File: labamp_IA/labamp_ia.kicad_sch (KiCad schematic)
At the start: 35 parts, among them J1 Conn_02x06_Odd_Even, J2 Conn_02x06_Odd_Even, J3 Conn_01x03, U1 ${SIM.PARAMS}, U2 ${SIM.PARAMS}, U3 THS4521ID

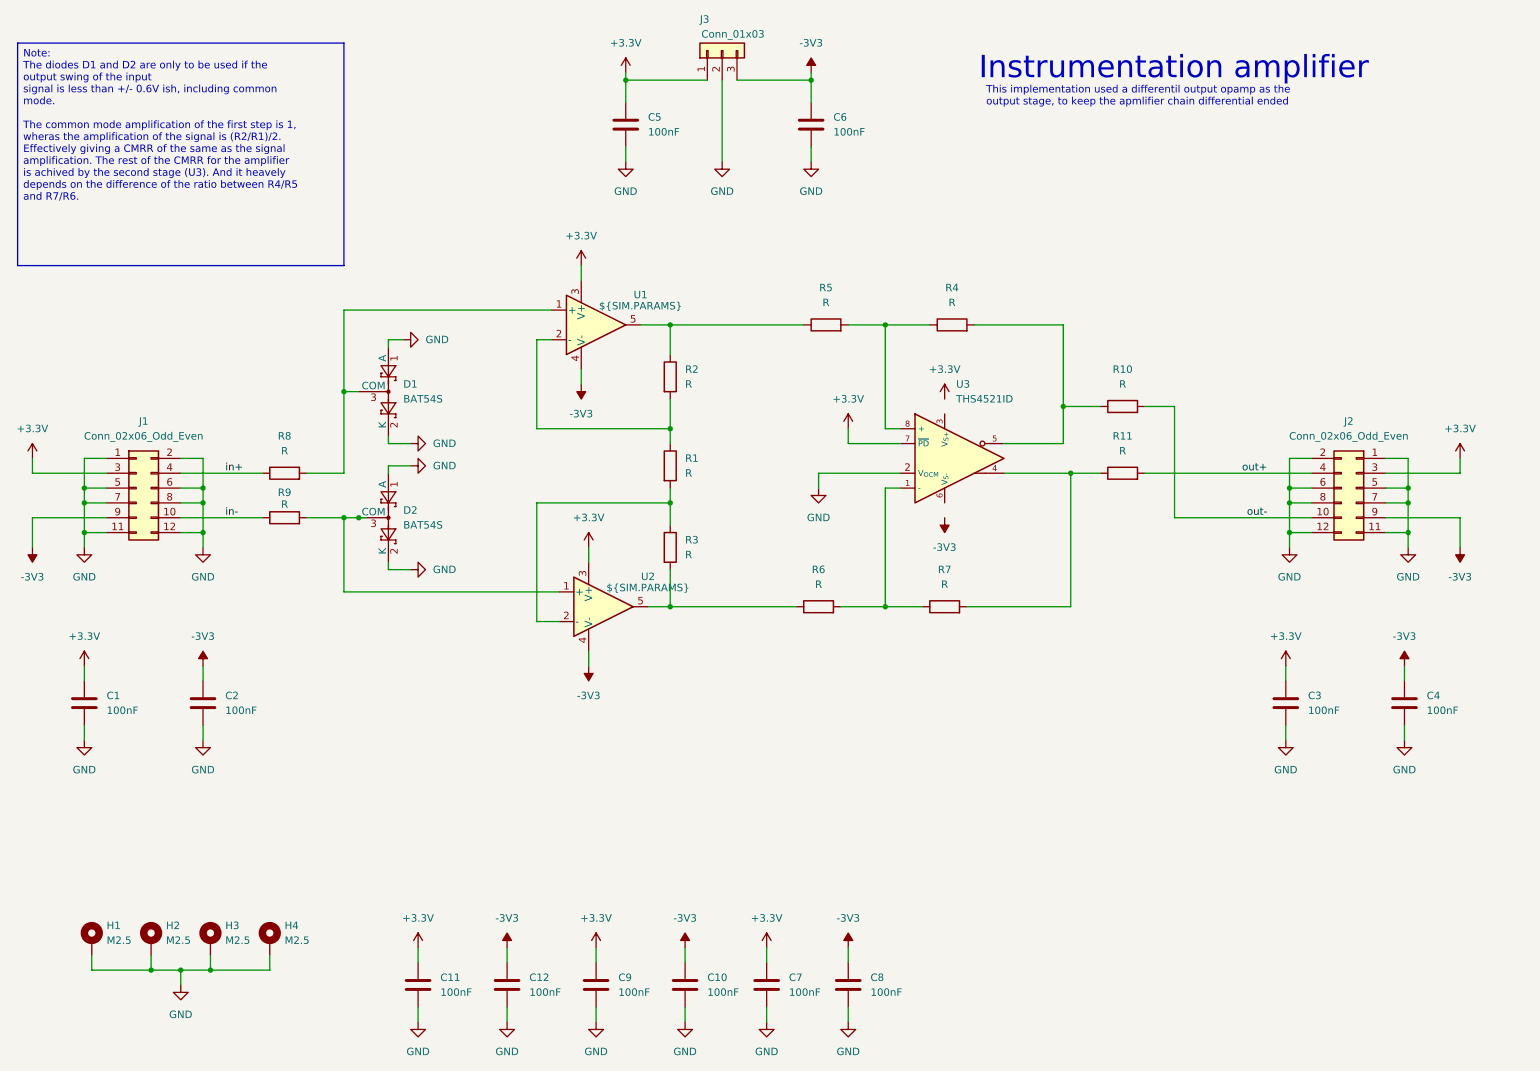
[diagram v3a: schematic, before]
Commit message: Routed PCB for IA. Added resistor network for high precition resistors.
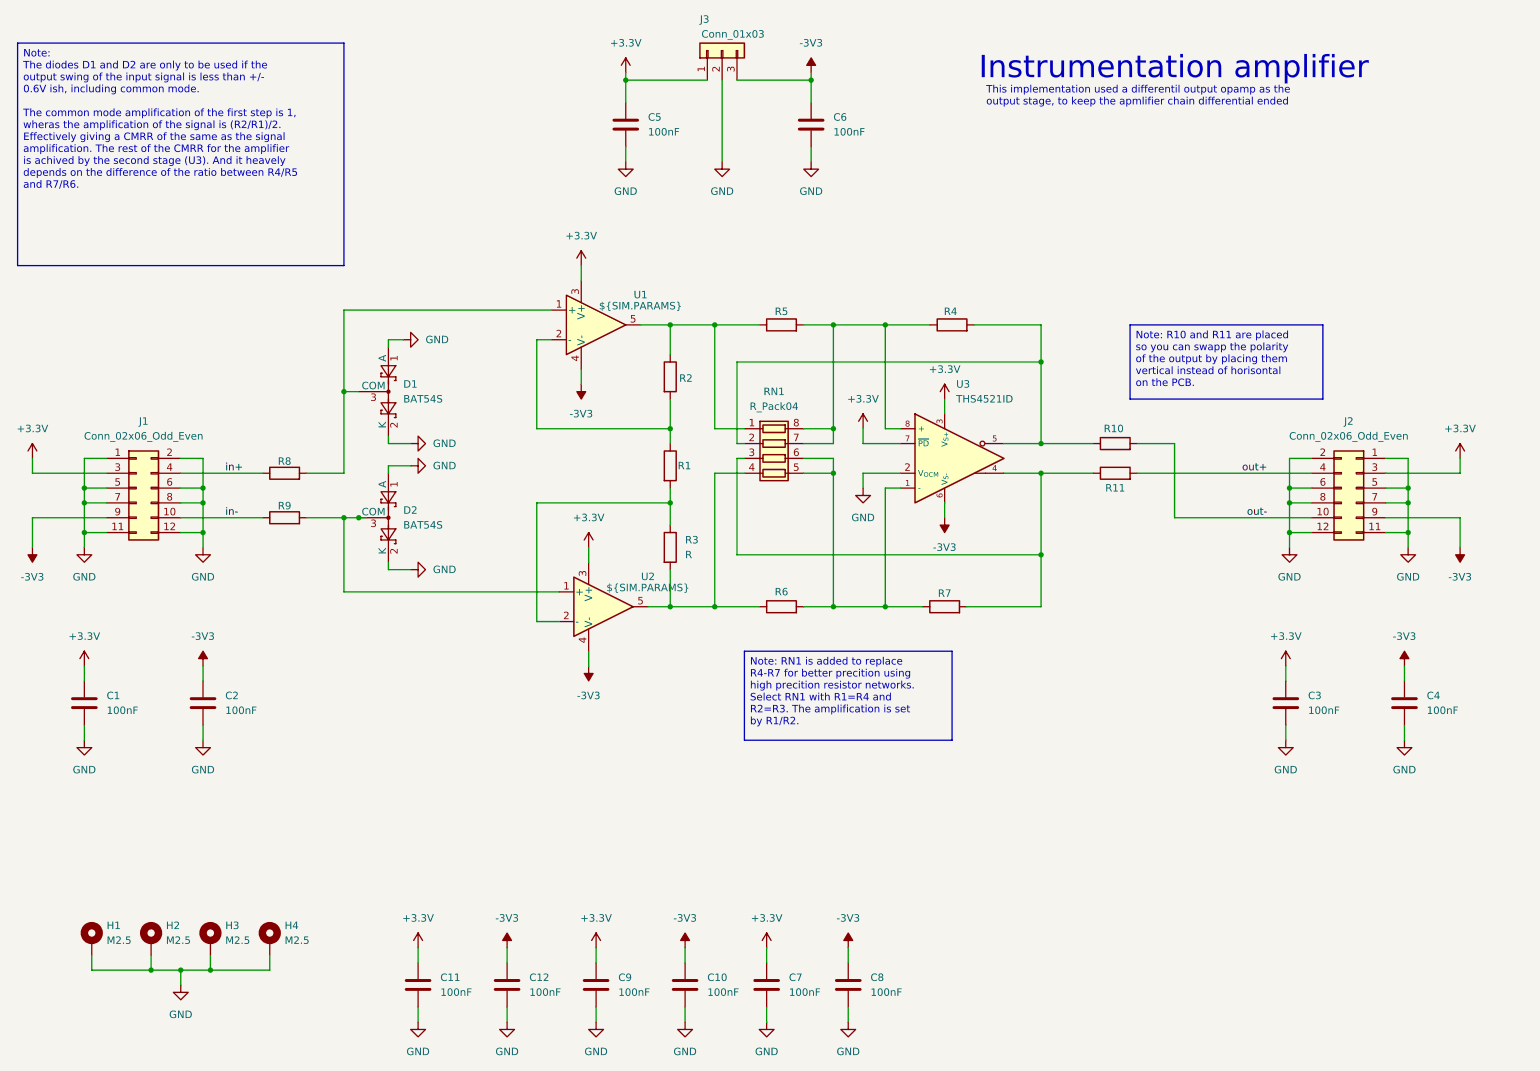
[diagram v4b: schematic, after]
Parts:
- added RN1: R_Pack04, Resistor_SMD:R_Array_Concave_4x0603, symbol Device:R_Pack04
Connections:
- net +3.3V: now also U3.3 (V_{S+})
- net -3V3: now also U3.6 (V_{S-})
- net at R6.2, R7.1, U3.1 (-): now also RN1.5 (R4.2), RN1.6 (R3.2)
- net at R11.1, R7.2, U3.4: now also RN1.3 (R3.1)
- net at R10.1, R4.2, U3.5: now also RN1.2 (R2.1)
- net at R4.1, R5.2, U3.8 (+): now also RN1.7 (R2.2), RN1.8 (R1.2)
- net at R3.2, R6.1, U2.5: now also RN1.4 (R4.1)
- net at R2.1, R5.1, U1.5: now also RN1.1 (R1.1)
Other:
- moved on the sheet: R10, R11, R5, R6

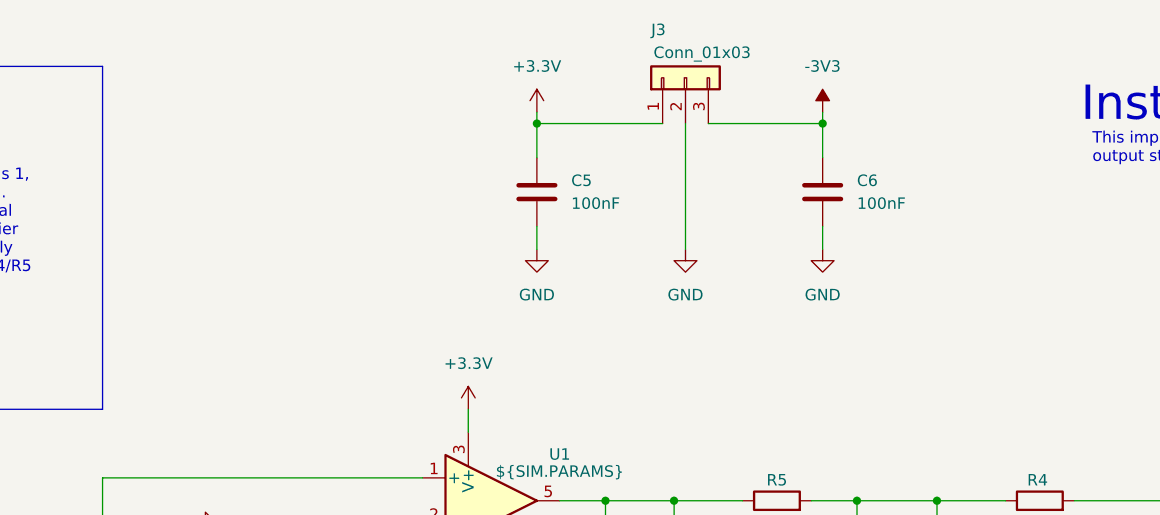
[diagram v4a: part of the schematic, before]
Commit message: Added virtual GND plane generator to IA
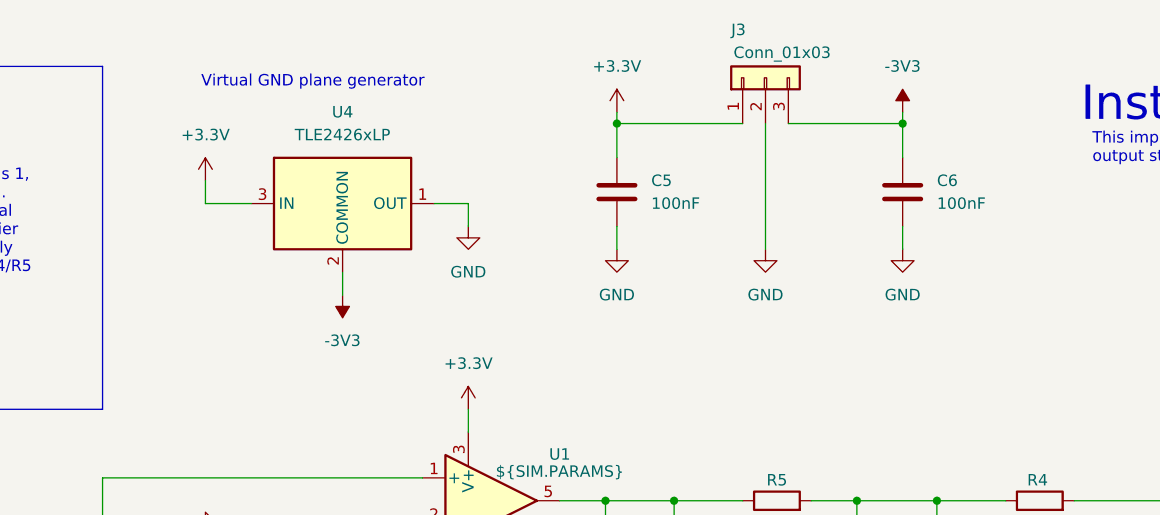
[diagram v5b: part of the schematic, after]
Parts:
- added U4: TLE2426xLP, Package_TO_SOT_THT:TO-92_Inline, symbol Reference_Voltage:TLE2426xLP
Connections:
- net +3.3V: now also U4.3 (IN)
- net -3V3: now also U4.2 (COMMON)
- net GND: now also U4.1 (OUT)
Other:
- note added: "Virtual GND plane generator"
- moved on the sheet: C5, C6, J3
